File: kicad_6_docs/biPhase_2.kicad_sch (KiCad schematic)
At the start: 5 parts, among them J1 IN_A, J2 IN_B, J3 OUT_A, J4 OUT_B

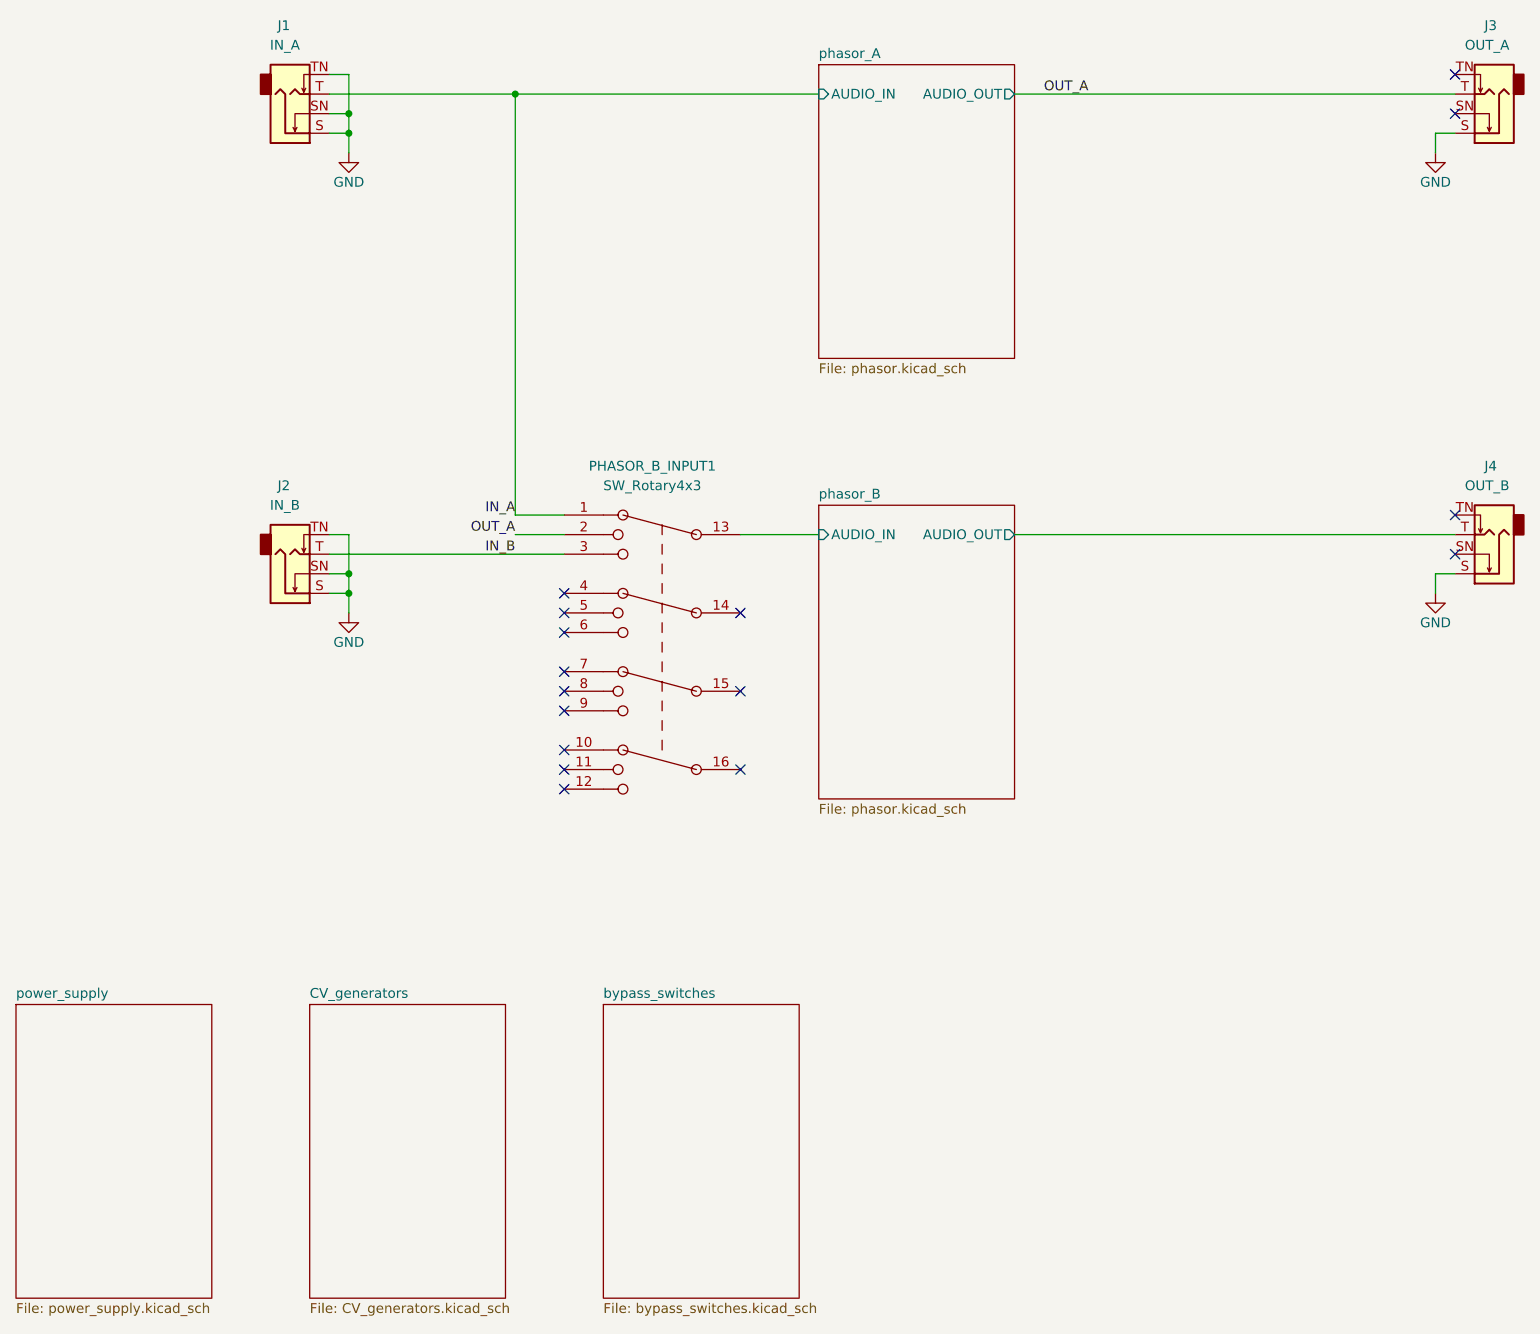
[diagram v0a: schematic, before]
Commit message: Fix power supply errors, tidy up schematic
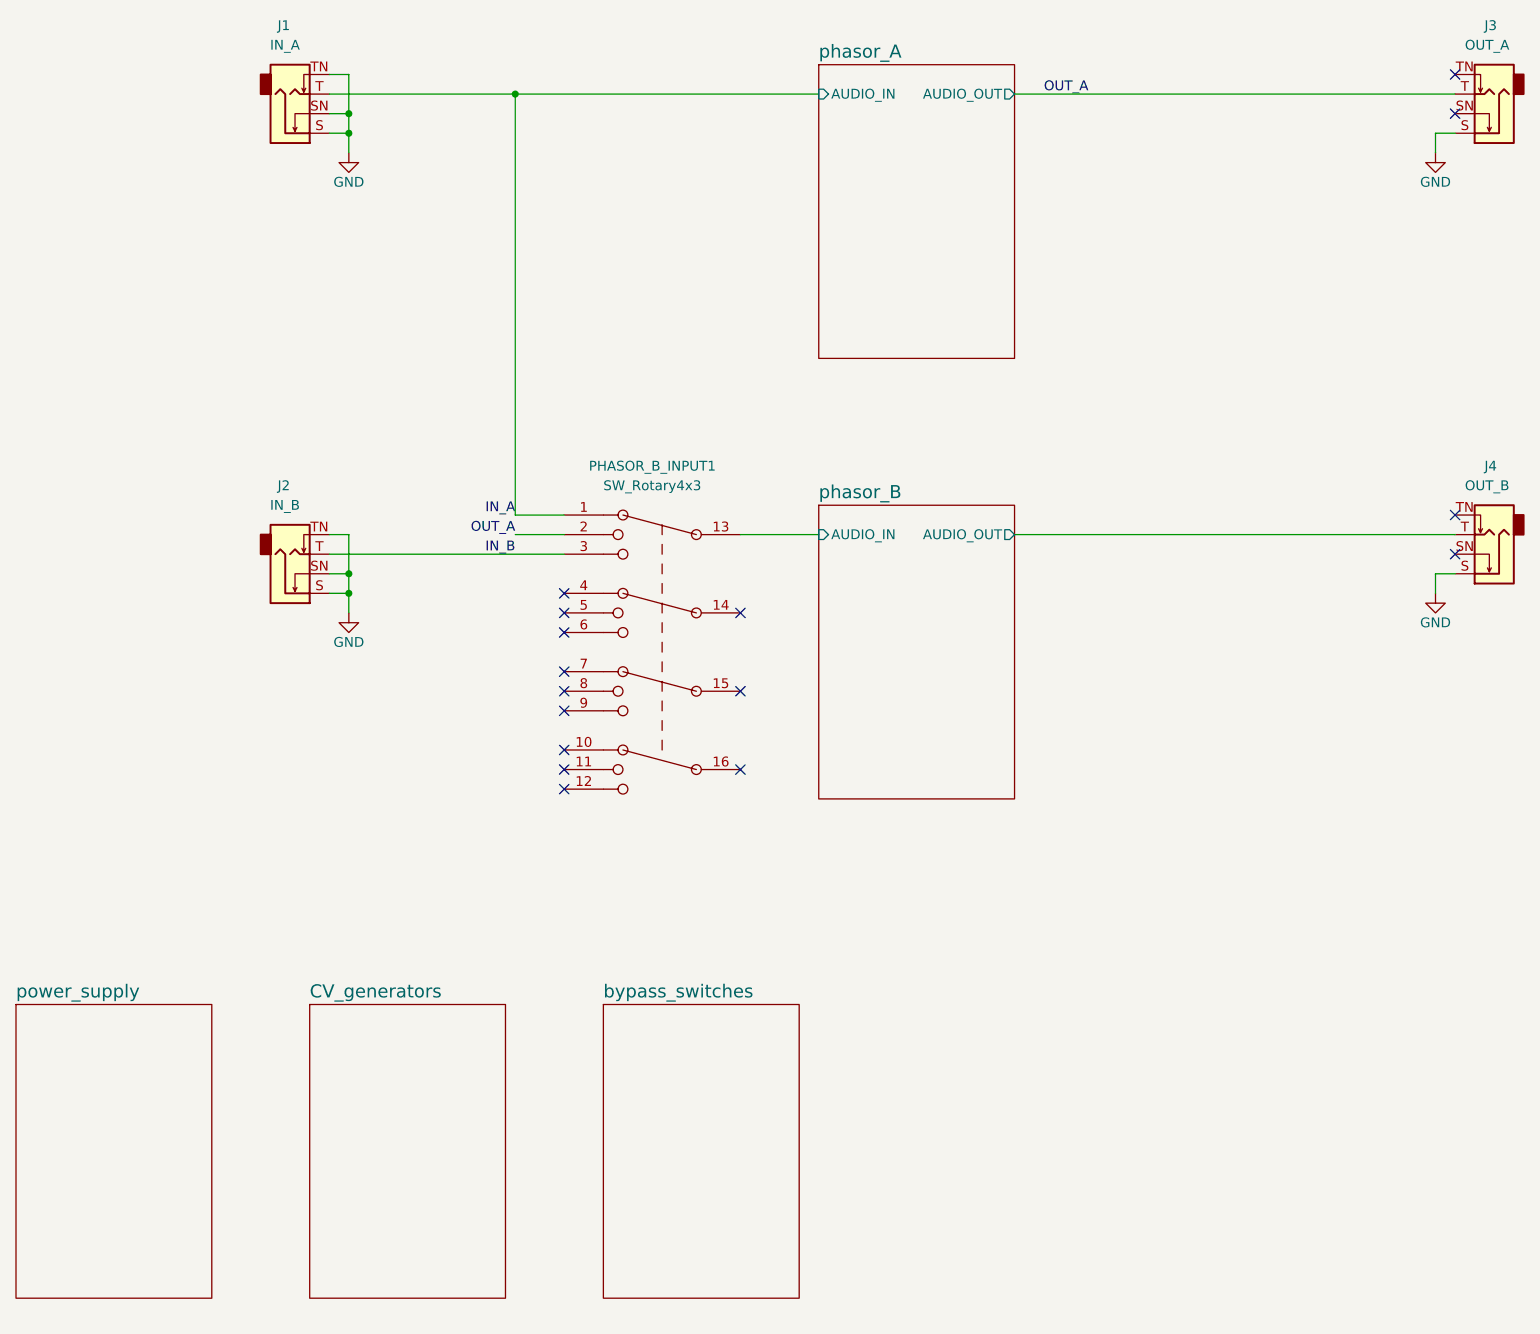
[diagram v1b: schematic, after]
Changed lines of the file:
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@@
   (title_block
     (title "Mu-Tron Bi-Phase near-clone")
-    (date "2022-01-14")
+    (date "2022-08-01")
     (rev "0")
     (comment 2 "creativecommons.org/licenses/by/4.0/")
@@
     (fill (color 0 0 0 0.0000))
     (property "Sheet name" "phasor_B" (id 0) (at 129.54 86.9184 0)
-      (effects (font (size 1.27 1.27)) (justify left bottom))
+      (effects (font (size 1.7 1.7)) (justify left bottom))
     )
     (property "Sheet file" "phasor.kicad_sch" (id 1) (at 129.54 126.3146 0)
-      (effects (font (size 1.27 1.27)) (justify left top))
+      (effects (font (size 1.27 1.27)) (justify left top) hide)
     )
     (pin "AUDIO_OUT" output (at 154.94 91.44 0)
@@
     (fill (color 0 0 0 0.0000))
     (property "Sheet name" "bypass_switches" (id 0) (at 101.6 151.6884 0)
-      (effects (font (size 1.27 1.27)) (justify left bottom))
+      (effects (font (size 1.7 1.7)) (justify left bottom))
     )
     (property "Sheet file" "bypass_switches.kicad_sch" (id 1) (at 101.6 191.0846 0)
-      (effects (font (size 1.27 1.27)) (justify left top))
+      (effects (font (size 1.27 1.27)) (justify left top) hide)
     )
   )
@@
     (fill (color 0 0 0 0.0000))
     (property "Sheet name" "power_supply" (id 0) (at 25.4 151.6884 0)
-      (effects (font (size 1.27 1.27)) (justify left bottom))
+      (effects (font (size 1.7 1.7)) (justify left bottom))
     )
     (property "Sheet file" "power_supply.kicad_sch" (id 1) (at 25.4 191.0846 0)
-      (effects (font (size 1.27 1.27)) (justify left top))
+      (effects (font (size 1.27 1.27)) (justify left top) hide)
     )
   )
@@
     (fill (color 0 0 0 0.0000))
     (property "Sheet name" "CV_generators" (id 0) (at 63.5 151.6884 0)
-      (effects (font (size 1.27 1.27)) (justify left bottom))
+      (effects (font (size 1.7 1.7)) (justify left bottom))
     )
     (property "Sheet file" "CV_generators.kicad_sch" (id 1) (at 63.5 191.0846 0)
-      (effects (font (size 1.27 1.27)) (justify left top))
+      (effects (font (size 1.27 1.27)) (justify left top) hide)
     )
   )
@@
     (fill (color 0 0 0 0.0000))
     (property "Sheet name" "phasor_A" (id 0) (at 129.54 29.7684 0)
-      (effects (font (size 1.27 1.27)) (justify left bottom))
+      (effects (font (size 1.7 1.7)) (justify left bottom))
     )
     (property "Sheet file" "phasor.kicad_sch" (id 1) (at 129.54 69.1646 0)
-      (effects (font (size 1.27 1.27)) (justify left top))
+      (effects (font (size 1.27 1.27)) (justify left top) hide)
     )
     (pin "AUDIO_OUT" output (at 154.94 34.29 0)
@@
     )
     (path "/9f4e8993-8a63-49e8-a372-f3335477401b/3a9ed25d-cf52-4b6f-867a-f4d9ddc8abb7"
-      (reference "RV13") (unit 1) (value "2k") (footprint "")
+      (reference "RV13") (unit 1) (value "5k") (footprint "")
     )
     (path "/9f4e8993-8a63-49e8-a372-f3335477401b/0037187d-afba-40fe-896c-61db36891028"
-      (reference "RV14") (unit 1) (value "2k") (footprint "")
+      (reference "RV14") (unit 1) (value "5k") (footprint "")
     )
     (path "/a00a4343-8da8-45c6-928f-bef4fe5d5b93/b1823a4f-e96f-438d-9402-c17cc7174fdd/d1990fe1-dde6-4a18-bcc0-c7c9343051d1"
